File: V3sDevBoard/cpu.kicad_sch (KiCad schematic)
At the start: 38 parts, among them U1 Allwinner_V3s, Y1 32768, Y2 24M

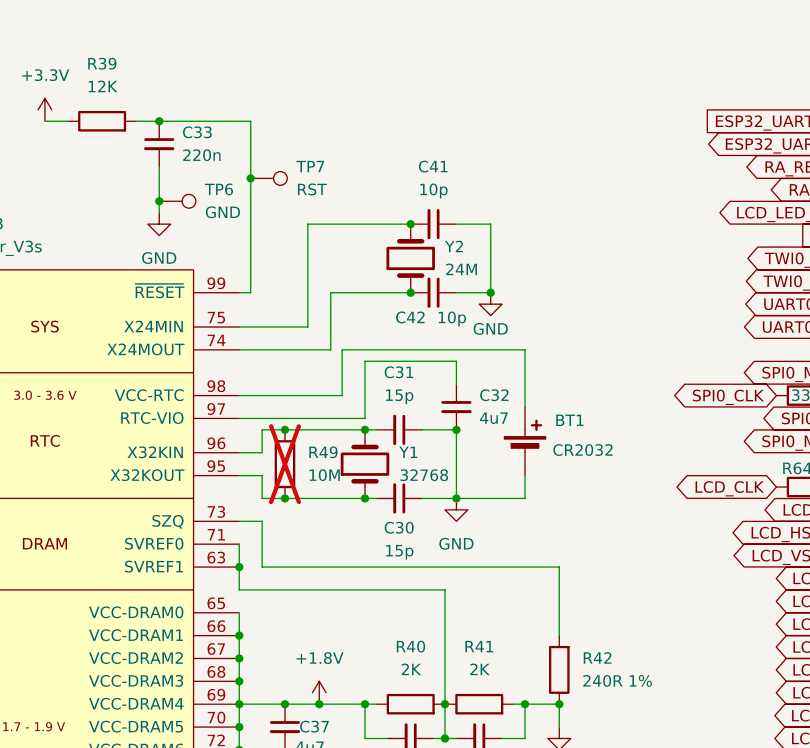
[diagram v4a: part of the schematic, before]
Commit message: first attempts to arrange components on a PCB
plus making footprints bme280&mpu6050 easier to hand solder.
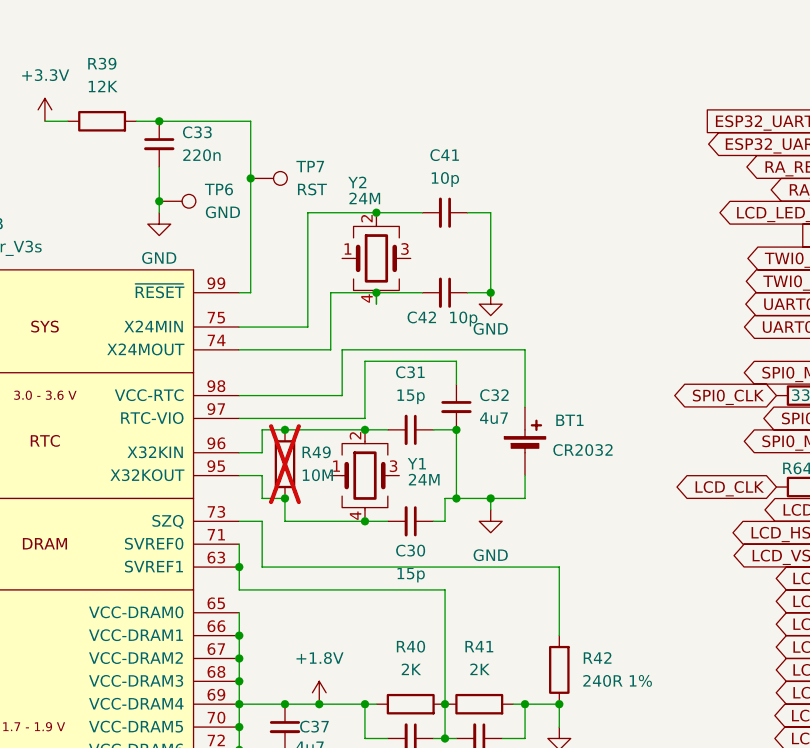
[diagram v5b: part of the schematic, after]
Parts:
- removed Y1: 32768, Crystal:Crystal_SMD_Abracon_ABS25-4Pin_8.0x3.8mm, symbol Device:Crystal
- removed Y2: 24M, Crystal:Crystal_HC49-4H_Vertical, symbol Device:Crystal
- added Y1, Y2: 24M, Crystal:Crystal_SMD_3225-4Pin_3.2x2.5mm_HandSoldering, symbol Device:Crystal_GND24
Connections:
- net at C30.2, R49.1, U1.95 (X32KOUT): now also Y1.4
- net at C31.2, R49.2, U1.96 (X32KIN): now also Y1.2
- net at C42.2, U1.74 (X24MOUT): now also Y2.4
- net at C41.2, U1.75 (X24MIN): now also Y2.2
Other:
- moved on the sheet: C30, C31, C41, C42

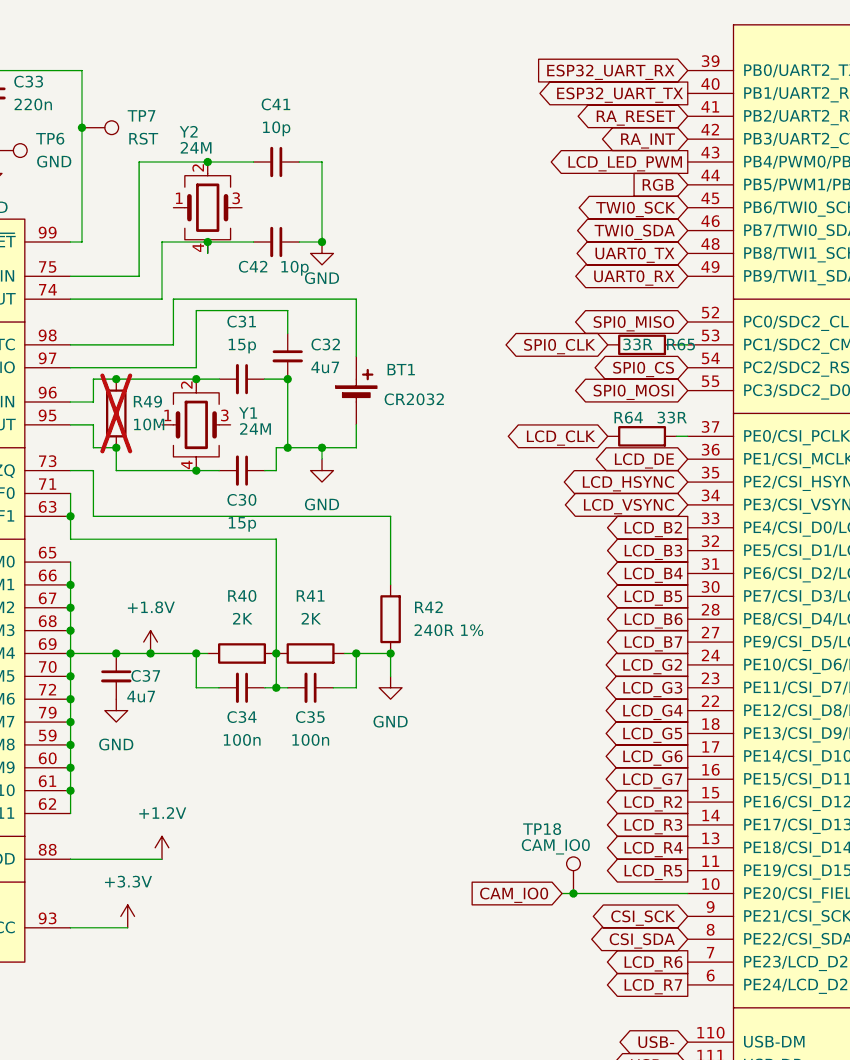
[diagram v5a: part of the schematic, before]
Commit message: completing pcb desgin
Returning to project after month away. Switching to 4-layer desgin on 3313 stackup sig-gnd-pow-sig, changing size of some passive to 0603, connecting all components, adding silkscreen.
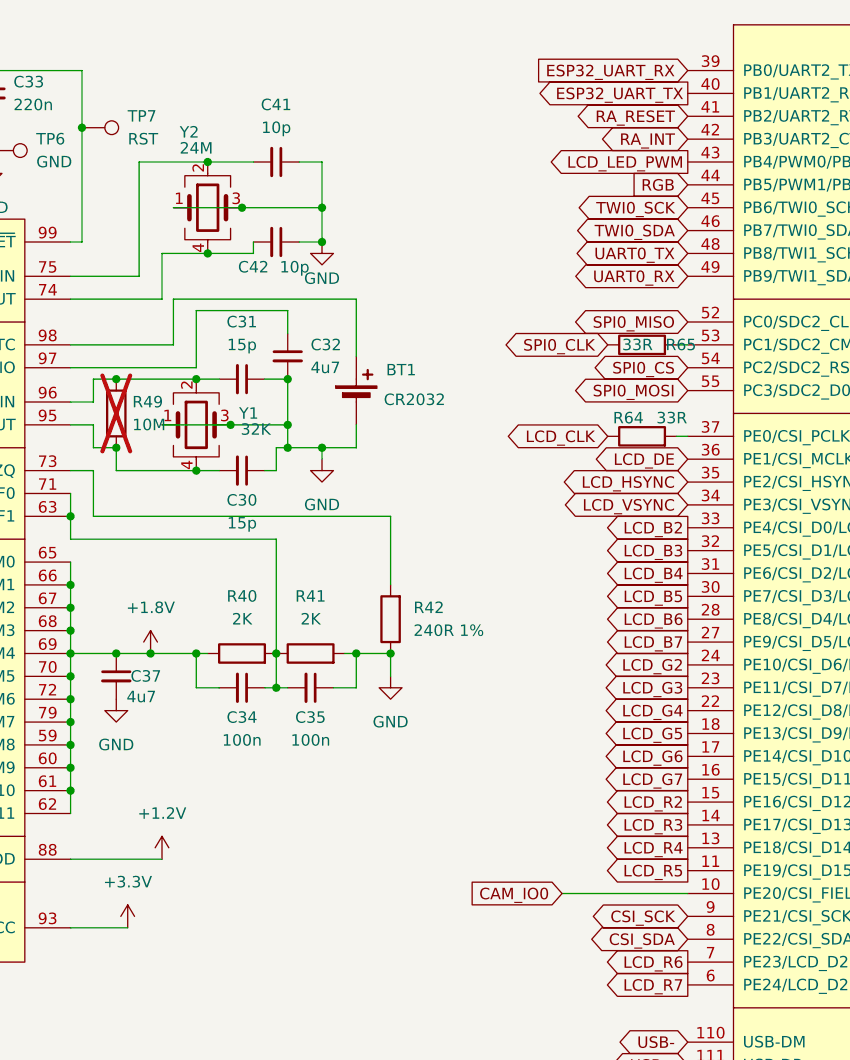
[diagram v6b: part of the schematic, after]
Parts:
- removed TP18: CAM_IO0, TestPoint:TestPoint_Pad_D1.0mm, symbol Connector:TestPoint
- BT1: footprint Battery:BatteryHolder_MYOUNG_BS-07-A1BJ001_CR2032 -> Connector_PinHeader_1.00mm:PinHeader_1x02_P1.00mm_Vertical_SMD_Pin1Right
- C30, C31, C33, C34, C35, C41, C42: footprint Capacitor_SMD:C_0805_2012Metric_Pad1.18x1.45mm_HandSolder -> Capacitor_SMD:C_0603_1608Metric_Pad1.08x0.95mm_HandSolder
- R29, R39, R40, R41, R42, R49: footprint Resistor_SMD:R_0805_2012Metric_Pad1.20x1.40mm_HandSolder -> Resistor_SMD:R_0603_1608Metric_Pad0.98x0.95mm_HandSolder
- Y1: value 24M -> 32K
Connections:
- net GND: now also Y1.1, Y1.3, Y2.1, Y2.3
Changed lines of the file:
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@@
 	)
 	(junction
-		(at 139.7 128.27)
-		(diameter 0)
-		(color 0 0 0 0)
-	)
-	(junction
 		(at 83.82 93.98)
 		(diameter 0)
@@
 	)
 	(junction
-		(at 20.32 73.66)
+		(at 101.6 76.2)
 		(diameter 0)
 		(color 0 0 0 0)
 	)
 	(junction
-		(at 88.9 71.12)
+		(at 20.32 73.66)
 		(diameter 0)
 		(color 0 0 0 0)
 	)
 	(junction
-		(at 99.06 55.88)
+		(at 88.9 71.12)
 		(diameter 0)
 		(color 0 0 0 0)
@@
 	)
 	(junction
+		(at 107.95 76.2)
+		(diameter 0)
+		(color 0 0 0 0)
+	)
+	(junction
 		(at 54.61 140.97)
 		(diameter 0)
@@
 	)
 	(junction
+		(at 111.76 52.07)
+		(diameter 0)
+		(color 0 0 0 0)
+	)
+	(junction
 		(at 85.09 43.18)
 		(diameter 0)
@@
 	)
 	(junction
+		(at 99.06 57.15)
+		(diameter 0)
+		(color 0 0 0 0)
+	)
+	(junction
 		(at 27.94 124.46)
 		(diameter 0)
@@
 	)
 	(junction
+		(at 102.87 52.07)
+		(diameter 0)
+		(color 0 0 0 0)
+	)
+	(junction
 		(at 97.79 81.28)
 		(diameter 0)
@@
 	(wire
 		(pts
-			(xy 107.95 78.74) (xy 107.95 71.12)
+			(xy 107.95 78.74) (xy 107.95 76.2)
 		)
 		(stroke
@@
 	(wire
 		(pts
-			(xy 111.76 55.88) (xy 111.76 46.99)
+			(xy 111.76 55.88) (xy 111.76 52.07)
 		)
 		(stroke
@@
 	(wire
 		(pts
+			(xy 95.25 52.07) (xy 102.87 52.07)
+		)
+		(stroke
+			(width 0)
+			(type default)
+		)
+	)
+	(wire
+		(pts
 			(xy 24.13 85.09) (xy 24.13 80.01)
 		)
@@
 	(wire
 		(pts
+			(xy 101.6 76.2) (xy 107.95 76.2)
+		)
+		(stroke
+			(width 0)
+			(type default)
+		)
+	)
+	(wire
+		(pts
 			(xy 24.13 64.77) (xy 27.94 64.77)
 		)
@@
 	(wire
 		(pts
+			(xy 111.76 52.07) (xy 111.76 46.99)
+		)
+		(stroke
+			(width 0)
+			(type default)
+		)
+	)
+	(wire
+		(pts
 			(xy 119.38 86.36) (xy 119.38 93.98)
 		)
@@
 	(wire
 		(pts
-			(xy 88.9 81.28) (xy 88.9 78.74)
+			(xy 102.87 52.07) (xy 111.76 52.07)
 		)
 		(stroke
@@
 	(wire
 		(pts
-			(xy 99.06 57.15) (xy 99.06 55.88)
+			(xy 88.9 81.28) (xy 88.9 78.74)
 		)
 		(stroke
@@
 	(wire
 		(pts
+			(xy 107.95 76.2) (xy 107.95 71.12)
+		)
+		(stroke
+			(width 0)
+			(type default)
+		)
+	)
+	(wire
+		(pts
 			(xy 106.68 101.6) (xy 106.68 105.41)
 		)
@@
 	(wire
 		(pts
-			(xy 93.98 62.23) (xy 93.98 55.88)
+			(xy 93.98 62.23) (xy 93.98 57.15)
 		)
 		(stroke
@@
 	(wire
 		(pts
-			(xy 93.98 55.88) (xy 99.06 55.88)
+			(xy 93.98 57.15) (xy 99.06 57.15)
 		)
 		(stroke
@@
 	(wire
 		(pts
-			(xy 138.43 128.27) (xy 139.7 128.27)
+			(xy 138.43 128.27) (xy 152.4 128.27)
 		)
 		(stroke
@@
 	(wire
 		(pts
-			(xy 139.7 128.27) (xy 152.4 128.27)
+			(xy 83.82 101.6) (xy 83.82 99.06)
 		)
 		(stroke
@@
 	(wire
 		(pts
-			(xy 83.82 101.6) (xy 83.82 99.06)
+			(xy 54.61 140.97) (xy 58.42 140.97)
 		)
 		(stroke
@@
 	(wire
 		(pts
-			(xy 54.61 140.97) (xy 58.42 140.97)
+			(xy 16.51 114.3) (xy 16.51 95.25)
 		)
 		(stroke
@@
 	(wire
 		(pts
-			(xy 16.51 114.3) (xy 16.51 95.25)
+			(xy 83.82 119.38) (xy 83.82 116.84)
 		)
 		(stroke
@@
 	(wire
 		(pts
-			(xy 83.82 119.38) (xy 83.82 116.84)
+			(xy 273.05 146.05) (xy 273.05 143.51)
 		)
 		(stroke
@@
 	(wire
 		(pts
-			(xy 273.05 146.05) (xy 273.05 143.51)
+			(xy 261.62 120.65) (xy 243.84 120.65)
 		)
 		(stroke
@@
 	(wire
 		(pts
-			(xy 261.62 120.65) (xy 243.84 120.65)
+			(xy 104.14 57.15) (xy 104.14 55.88)
 		)
 		(stroke
@@
 	(wire
 		(pts
-			(xy 99.06 55.88) (xy 104.14 55.88)
+			(xy 99.06 57.15) (xy 104.14 57.15)
 		)
 		(stroke
@@
 	(wire
 		(pts
+			(xy 93.98 76.2) (xy 101.6 76.2)
+		)
+		(stroke
+			(width 0)
+			(type default)
+		)
+	)
+	(wire
+		(pts
 			(xy 105.41 81.28) (xy 106.68 81.28)
 		)
@@
 			)
 		)
-		(property "Footprint" "Resistor_SMD:R_0805_2012Metric_Pad1.20x1.40mm_HandSolder"
+		(property "Footprint" "Resistor_SMD:R_0603_1608Metric_Pad0.98x0.95mm_HandSolder"
 			(at 90.678 74.93 90)
 			(effects
@@
 			)
 		)
-		(property "Footprint" "Capacitor_SMD:C_0805_2012Metric_Pad1.18x1.45mm_HandSolder"
+		(property "Footprint" "Capacitor_SMD:C_0603_1608Metric_Pad1.08x0.95mm_HandSolder"
 			(at 102.87 105.41 0)
 			(effects
@@
 			)
 		)
-		(property "Footprint" "Resistor_SMD:R_0805_2012Metric_Pad1.20x1.40mm_HandSolder"
+		(property "Footprint" "Resistor_SMD:R_0603_1608Metric_Pad0.98x0.95mm_HandSolder"
 			(at 102.87 103.378 90)
 			(effects
@@
 			)
 		)
-		(property "Footprint" "Resistor_SMD:R_0805_2012Metric_Pad1.20x1.40mm_HandSolder"
+		(property "Footprint" "Resistor_SMD:R_0603_1608Metric_Pad0.98x0.95mm_HandSolder"
 			(at 110.49 103.378 90)
 			(effects
@@
 			)
 		)
-		(property "Value" "24M"
+		(property "Value" "32K"
 			(at 104.394 76.708 0)
 			(effects
@@
 			)
 		)
-		(property "Footprint" "Capacitor_SMD:C_0805_2012Metric_Pad1.18x1.45mm_HandSolder"
+		(property "Footprint" "Capacitor_SMD:C_0603_1608Metric_Pad1.08x0.95mm_HandSolder"
 			(at 102.87 81.28 0)
 			(effects
@@
 			)
 		)
-		(property "Footprint" "Capacitor_SMD:C_0805_2012Metric_Pad1.18x1.45mm_HandSolder"
+		(property "Footprint" "Capacitor_SMD:C_0603_1608Metric_Pad1.08x0.95mm_HandSolder"
 			(at 102.87 71.12 0)
 			(effects
@@
 			)
 		)
-		(property "Footprint" "Capacitor_SMD:C_0805_2012Metric_Pad1.18x1.45mm_HandSolder"
+		(property "Footprint" "Capacitor_SMD:C_0603_1608Metric_Pad1.08x0.95mm_HandSolder"
 			(at 106.68 55.88 0)
 			(effects
@@
 			)
 		)
-		(property "Footprint" "Capacitor_SMD:C_0805_2012Metric_Pad1.18x1.45mm_HandSolder"
+		(property "Footprint" "Capacitor_SMD:C_0603_1608Metric_Pad1.08x0.95mm_HandSolder"
 			(at 106.68 46.99 0)
 			(effects
@@
 			)
 		)
-		(property "Footprint" "Resistor_SMD:R_0805_2012Metric_Pad1.20x1.40mm_HandSolder"
+		(property "Footprint" "Resistor_SMD:R_0603_1608Metric_Pad0.98x0.95mm_HandSolder"
 			(at 258.572 142.24 90)
 			(effects
@@
 			)
 		)
-		(property "Footprint" "Resistor_SMD:R_0805_2012Metric_Pad1.20x1.40mm_HandSolder"
+		(property "Footprint" "Resistor_SMD:R_0603_1608Metric_Pad0.98x0.95mm_HandSolder"
 			(at 121.158 97.79 90)
 			(effects
@@
 			)
 		)
-		(property "Footprint" "Capacitor_SMD:C_0805_2012Metric_Pad1.18x1.45mm_HandSolder"
+		(property "Footprint" "Capacitor_SMD:C_0603_1608Metric_Pad1.08x0.95mm_HandSolder"
 			(at 110.49 105.41 0)
 			(effects
@@
 			)
 		)
-		(property "Footprint" "Resistor_SMD:R_0805_2012Metric_Pad1.20x1.40mm_HandSolder"
+		(property "Footprint" "Resistor_SMD:R_0603_1608Metric_Pad0.98x0.95mm_HandSolder"
 			(at 68.58 38.608 90)
 			(effects
@@
 	)
 	(symbol
-		(lib_id "Connector:TestPoint")
-		(at 139.7 128.27 0)
-		(unit 1)
-		(exclude_from_sim no)
-		(in_bom yes)
-		(on_board yes)
-		(dnp no)
-		(property "Reference" "TP18"
-			(at 134.112 121.158 0)
-			(effects
-				(font
-					(size 1.27 1.27)
-				)
-				(justify left)
-			)
-		)
-		(property "Value" "CAM_IO0"
-			(at 133.858 122.936 0)
-			(effects
-				(font
-					(size 1.27 1.27)
-				)
-				(justify left)
-			)
-		)
-		(property "Footprint" "TestPoint:TestPoint_Pad_D1.0mm"
-			(at 144.78 128.27 0)
-			(effects
-				(font
-					(size 1.27 1.27)
-				)
-				(hide yes)
-			)
-		)
-		(property "Datasheet" "~"
-			(at 144.78 128.27 0)
-			(effects
-				(font
-					(size 1.27 1.27)
-				)
-				(hide yes)
-			)
-		)
-		(property "Description" "test point"
-			(at 139.7 128.27 0)
-			(effects
-				(font
-					(size 1.27 1.27)
-				)
-				(hide yes)
-			)
-		)
-		(pin "1"
-		)
-		(instances
-			(project "V3sDevBoard"
-				(path "/e07febb4-5889-4da3-b279-3be53a5a6756/68c96adc-b146-438e-b3a7-b1f90739e044"
-					(reference "TP18")
-					(unit 1)
-				)
-			)
-		)
-	)
-	(symbol
 		(lib_id "Device:C_Small")
 		(at 107.95 68.58 0)
@@
 			)
 		)
-		(property "Footprint" "Battery:BatteryHolder_MYOUNG_BS-07-A1BJ001_CR2032"
+		(property "Footprint" "Connector_PinHeader_1.00mm:PinHeader_1x02_P1.00mm_Vertical_SMD_Pin1Right"
 			(at 104.394 71.628 90)
 			(effects
@@
 			)
 		)
-		(property "Footprint" "Capacitor_SMD:C_0805_2012Metric_Pad1.18x1.45mm_HandSolder"
+		(property "Footprint" "Capacitor_SMD:C_0603_1608Metric_Pad1.08x0.95mm_HandSolder"
 			(at 74.93 39.37 0)
 			(effects

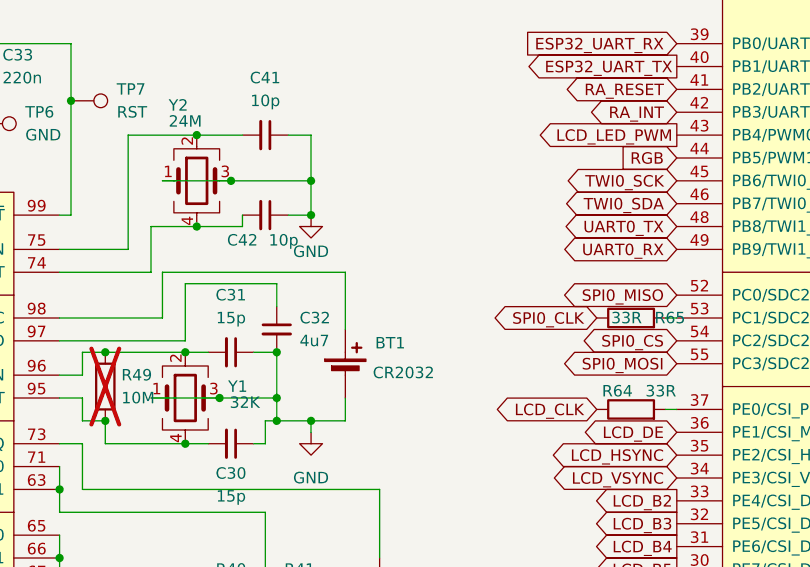
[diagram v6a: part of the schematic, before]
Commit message: fixing errors in revA
Fixing:
- Ther was mistake in SDIO for SDCard. Swaped data lines.
- RTC didn't have power without battery.
Updating readme.
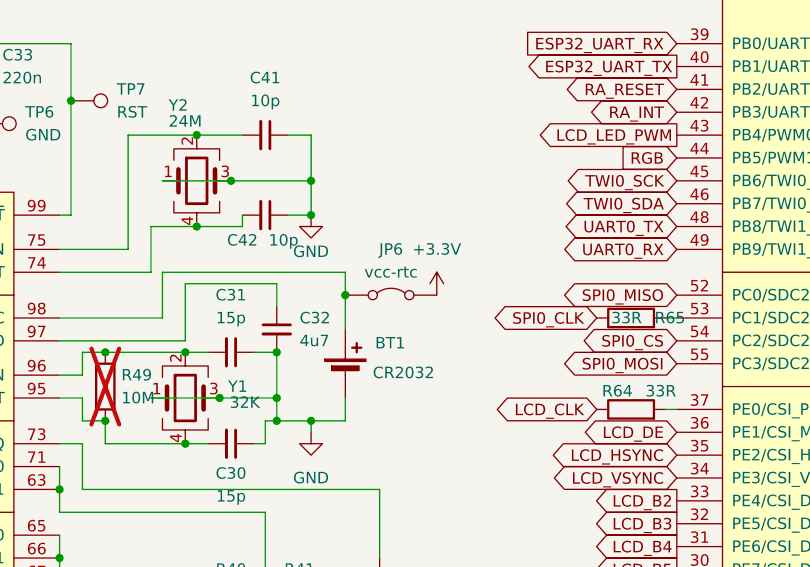
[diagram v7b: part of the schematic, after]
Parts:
- added JP6: vcc-rtc, Jumper:SolderJumper-2_P1.3mm_Bridged_RoundedPad1.0x1.5mm, symbol Jumper:Jumper_2_Bridged
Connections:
- net +3.3V: now also JP6.2 (B)
- net at BT1.1 (+), U1.98 (VCC-RTC): now also JP6.1 (A)
